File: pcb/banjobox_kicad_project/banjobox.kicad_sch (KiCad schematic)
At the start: 17 parts, among them SW1 RotaryEncoder_Switch, U1 SHT31-DIS, U2 MOUDLE-SEEEDUINO-XIAO, U3 ER_OLEDM0.91_1x-I2C, U4 PAM8302AAY

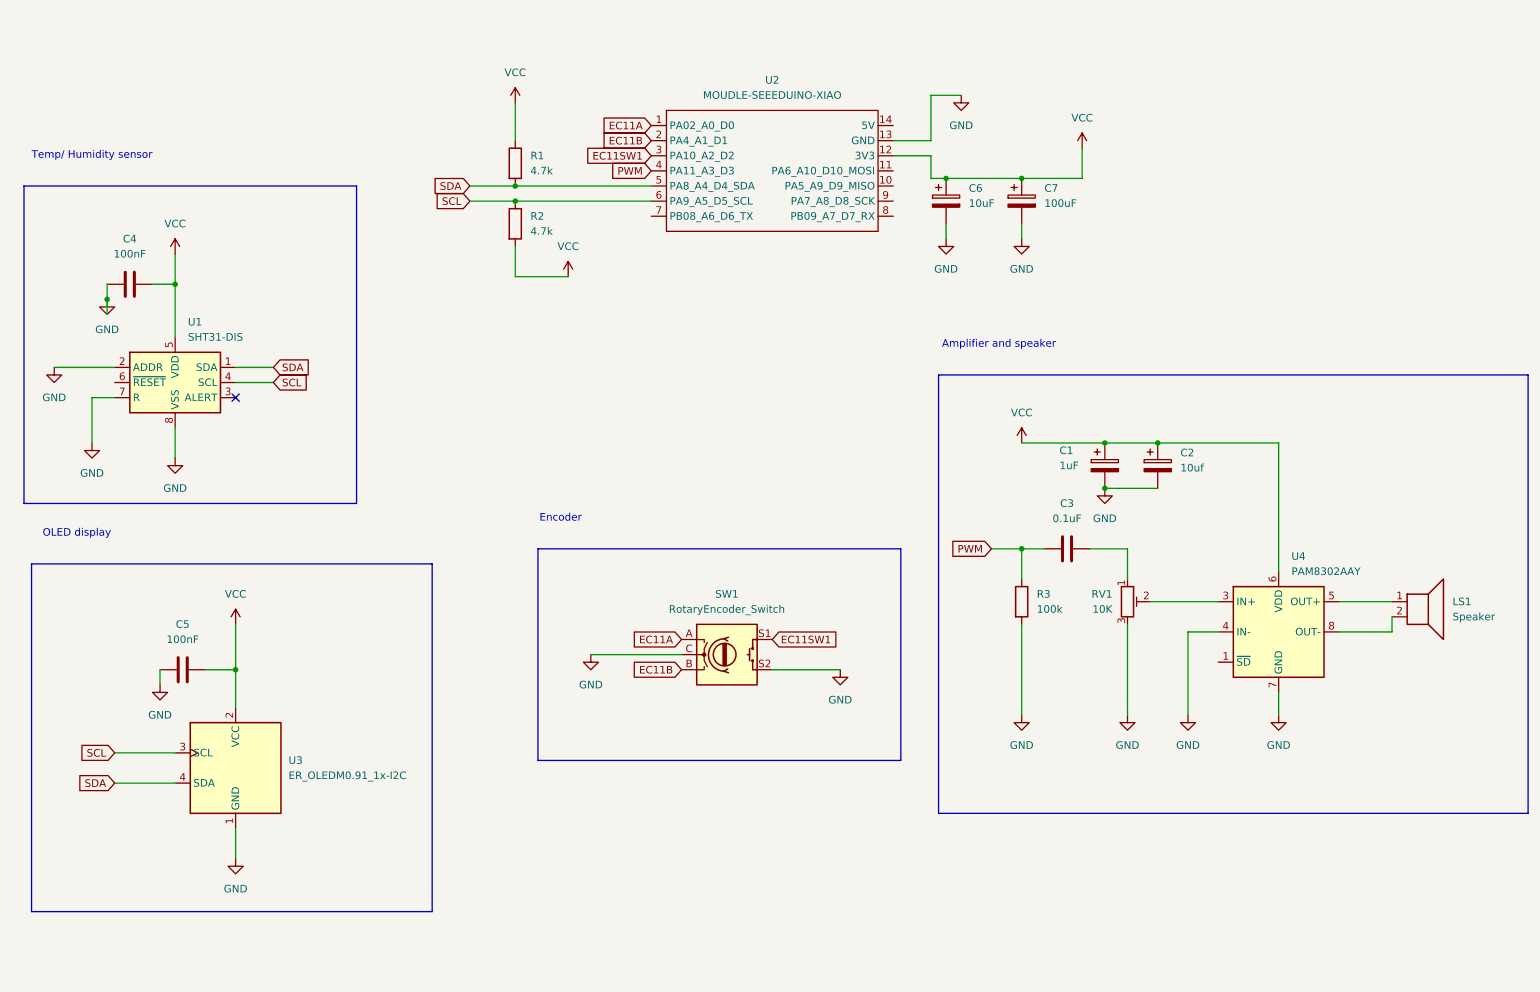
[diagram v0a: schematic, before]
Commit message: added voltage regulator to schematic and finished assigning footprints
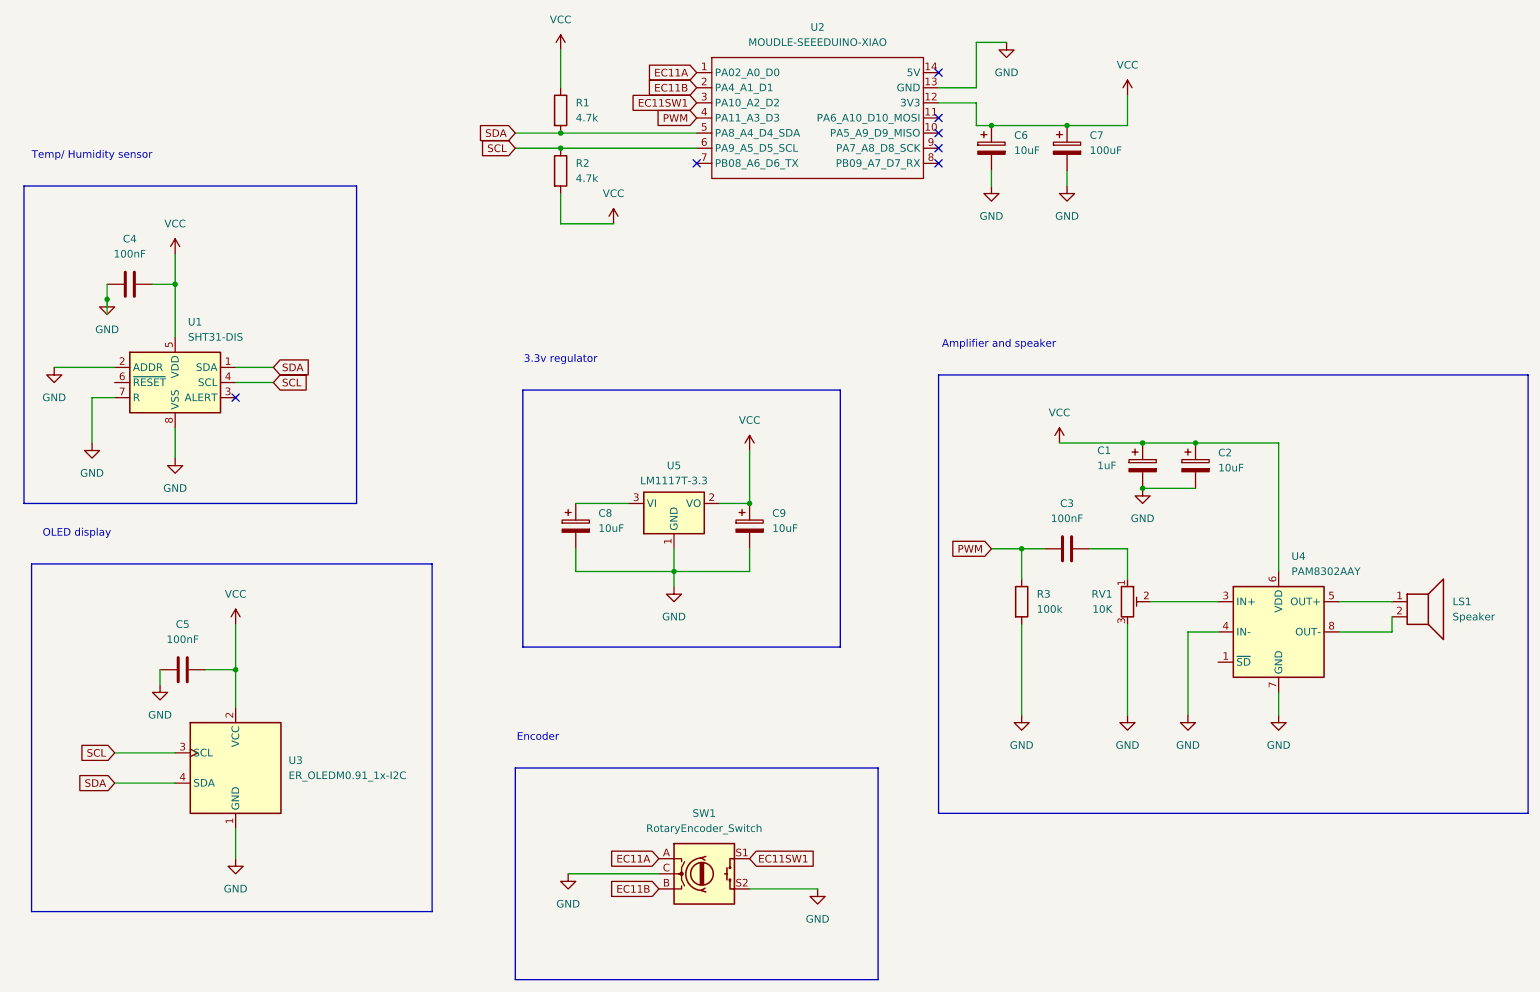
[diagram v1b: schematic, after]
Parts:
- added C8, C9: 10uF, Capacitor_THT:CP_Radial_D6.3mm_P2.50mm, symbol Device:C_Polarized
- added U5: LM1117T-3.3, Package_TO_SOT_THT:TO-220-3_Vertical, symbol Regulator_Linear:LM1117T-3.3
- C1, C6, C7: footprint (none) -> Capacitor_THT:CP_Radial_D6.3mm_P2.50mm
- C2: value 10uf -> 10uF; footprint (none) -> Capacitor_THT:CP_Radial_D6.3mm_P2.50mm
- C3: value 0.1uF -> 100nF; footprint (none) -> Capacitor_THT:C_Disc_D3.4mm_W2.1mm_P2.50mm
- C4, C5: footprint (none) -> Capacitor_THT:C_Disc_D3.4mm_W2.1mm_P2.50mm
- R1, R2, R3: footprint (none) -> Resistor_THT:R_Axial_DIN0207_L6.3mm_D2.5mm_P7.62mm_Horizontal
- RV1: footprint (none) -> Potentiometer_THT:Potentiometer_Runtron_RM-065_Vertical
- SW1: footprint (none) -> Rotary_Encoder:RotaryEncoder_Alps_EC11E-Switch_Vertical_H20mm
- U2: footprint (none) -> footprints:XIAO-Generic-Hybrid-14P-2.54-21X17.8MM
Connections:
- net GND: now also C8.2, C9.2, U5.1 (GND)
- net VCC: now also C9.1, U5.2 (VO)
- new net: C8.1, U5.3 (VI)
- no-connect marks 1 -> 7
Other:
- note added: "3.3v regulator"
- moved on the sheet: C1, C2, C6, C7, R1, R2, SW1, U2

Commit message: removed R pin from SHT31 to better suit breakout board
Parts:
- removed C6: 10uF, Capacitor_THT:CP_Radial_D6.3mm_P2.50mm, symbol Device:C_Polarized
- removed U4: PAM8302AAY, Package_DFN_QFN:DFN-8-1EP_3x3mm_P0.65mm_EP1.55x2.4mm, symbol Amplifier_Audio:PAM8302AAY
- added U6: PAM8302AAD, Package_SO:SOIC-8_3.9x4.9mm_P1.27mm, symbol Amplifier_Audio:PAM8302AAD
- U1: footprint Sensor_Humidity:Sensirion_DFN-8-1EP_2.5x2.5mm_P0.5mm_EP1.1x1.7mm -> (none)
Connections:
- net GND: now also U6.4 (IN-), U6.7 (GND); no longer U1.7 (R)
- net VCC: now also U6.6 (VDD)
- net +5V: now reaches C8.1, U5.3 (VI)
- net at RV1.2: now also U6.3 (IN+)
- net at LS1.1: now also U6.5 (OUT+)
- net at LS1.2: now also U6.8 (OUT-)
- no-connect marks 7 -> 10
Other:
- moved on the sheet: C7

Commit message: assigned new footprints (pinheader) and more progress on pcb
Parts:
- U1: footprint (none) -> Connector_PinHeader_2.54mm:PinHeader_1x06_P2.54mm_Vertical
- renumbered C4 to C1, C5 to C2, C8 to C3, C9 to C4, C7 to C5, C3 to C6, C1 to C7, C2 to C8, U3 to U2, U5 to U3, U2 to U4, U6 to U5
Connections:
- net SCL: now also U1.3 (SCL); no longer U1.4 (SCL)
- net SDA: now also U1.4 (SDA); no longer U1.1 (SDA)
- net VCC: now also U1.1 (VDD); no longer U1.5 (VDD)
- net +5V renamed +BATT
- net GND renamed -BATT
- net -BATT: now also U1.5 (ADDR); no longer U1.8 (VSS)

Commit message: routed pcb
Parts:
- added TP1, TP2, TP3, TP4: TestPoint, TestPoint:TestPoint_THTPad_D3.0mm_Drill1.5mm, symbol Connector:TestPoint
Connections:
- net +BATT: now also TP1.1
- net -BATT: now also TP2.1
- net PWM: now also U4.10 (PA5_A9_D9_MISO); no longer U4.4 (PA11_A3_D3)
- net at LS1.1, U5.5 (OUT+): now also TP3.1
- net at LS1.2, U5.8 (OUT-): now also TP4.1
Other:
- moved on the sheet: C5
